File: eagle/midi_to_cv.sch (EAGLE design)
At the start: 45 parts, among them IC2 4504N, IC3 4099N, U1 ATMEGA328P_PDIP

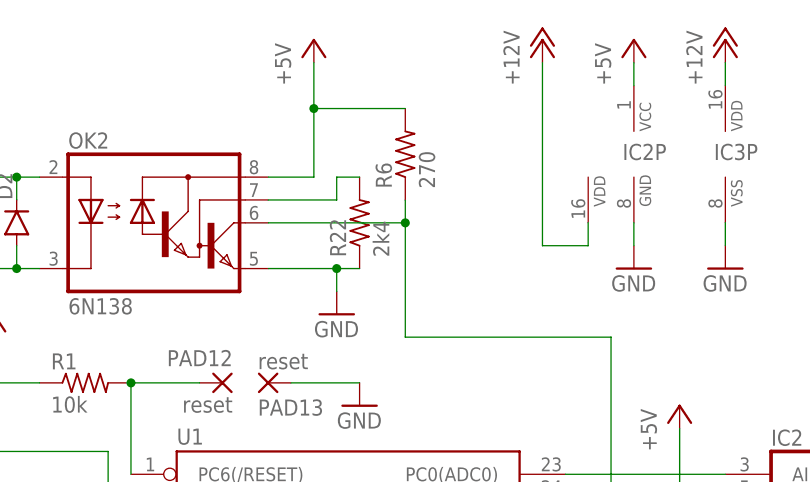
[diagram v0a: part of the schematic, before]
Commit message: wider traces and starting distro board
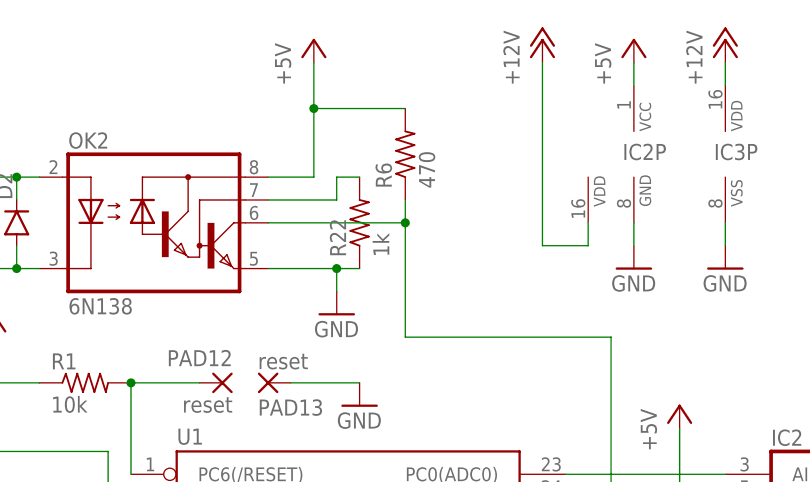
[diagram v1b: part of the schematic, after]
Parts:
- R22: value 2k4 -> 1k
- R6: value 270 -> 470
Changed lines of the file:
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@@
 <?xml version="1.0" encoding="utf-8"?>
 <!DOCTYPE eagle SYSTEM "eagle.dtd">
-<eagle version="7.2.0">
+<eagle version="7.1.0">
 <drawing>
 <settings>
@@
 <part name="D2" library="SparkFun-DiscreteSemi" deviceset="DIODE" device="1N4148"/>
 <part name="R5" library="rcl" deviceset="R-US_" device="0207/10" value="220"/>
-<part name="R6" library="rcl" deviceset="R-US_" device="0207/10" value="270"/>
+<part name="R6" library="rcl" deviceset="R-US_" device="0207/10" value="470"/>
 <part name="P+6" library="supply1" deviceset="+5V" device=""/>
 <part name="MIDI_IN" library="con-molex" deviceset="22-23-2021" device=""/>
@@
 <part name="JP2" library="pinhead" deviceset="PINHD-1X8" device=""/>
 <part name="JP3" library="pinhead" deviceset="PINHD-1X8" device=""/>
-<part name="R22" library="rcl" deviceset="R-US_" device="0207/10" value="2k4"/>
+<part name="R22" library="rcl" deviceset="R-US_" device="0207/10" value="1k"/>
 <part name="LED" library="con-molex" deviceset="22-23-2021" device=""/>
 <part name="GND1" library="supply1" deviceset="GND" device=""/>

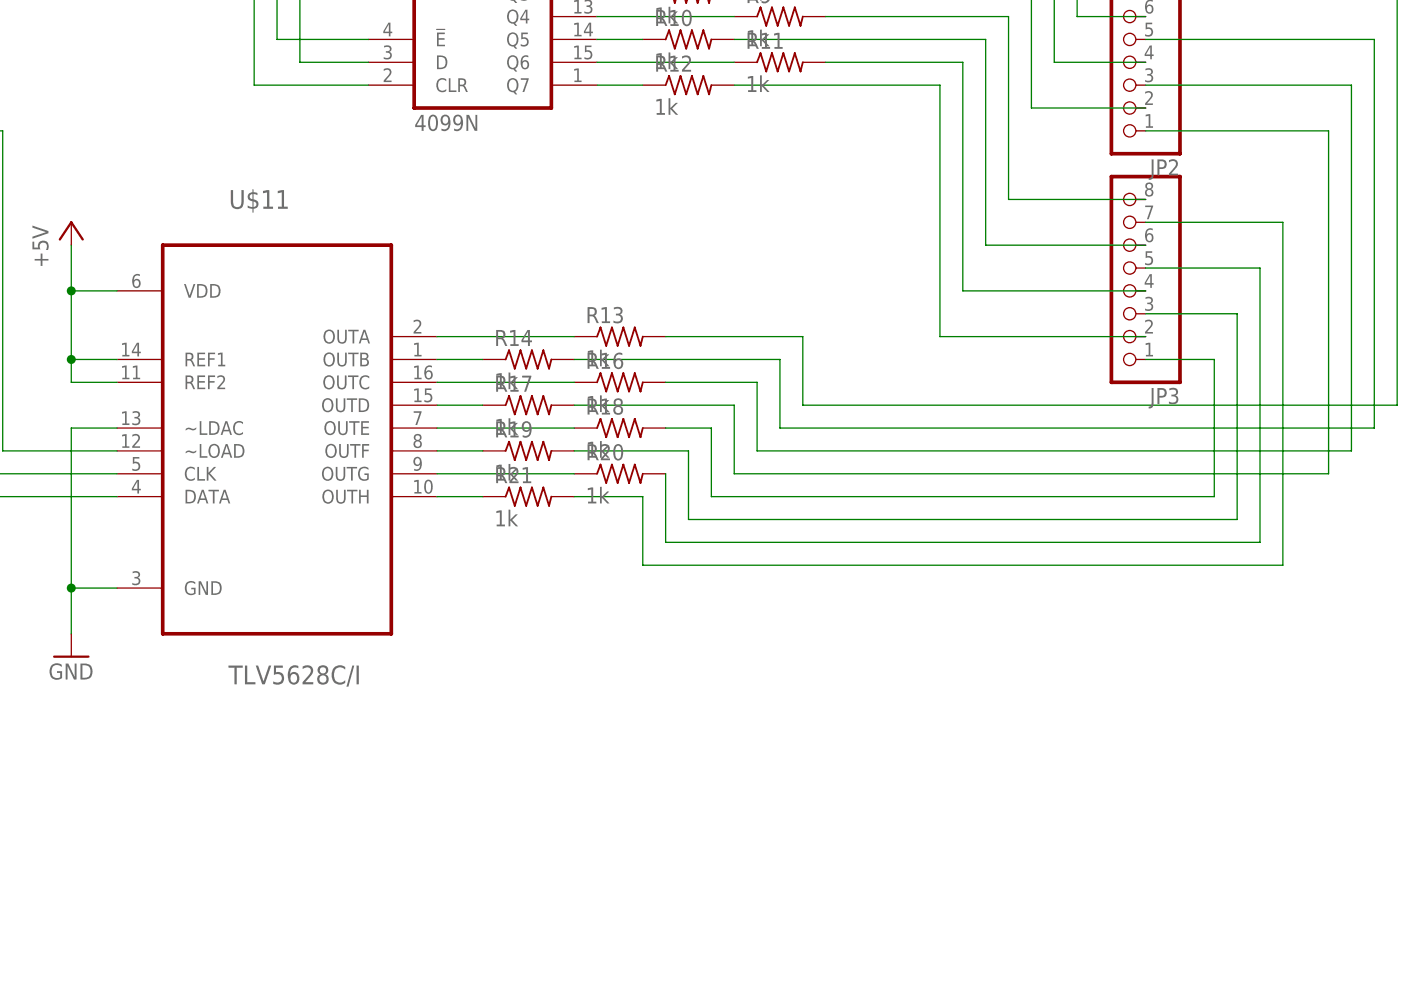
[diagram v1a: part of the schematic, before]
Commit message: adding opamps
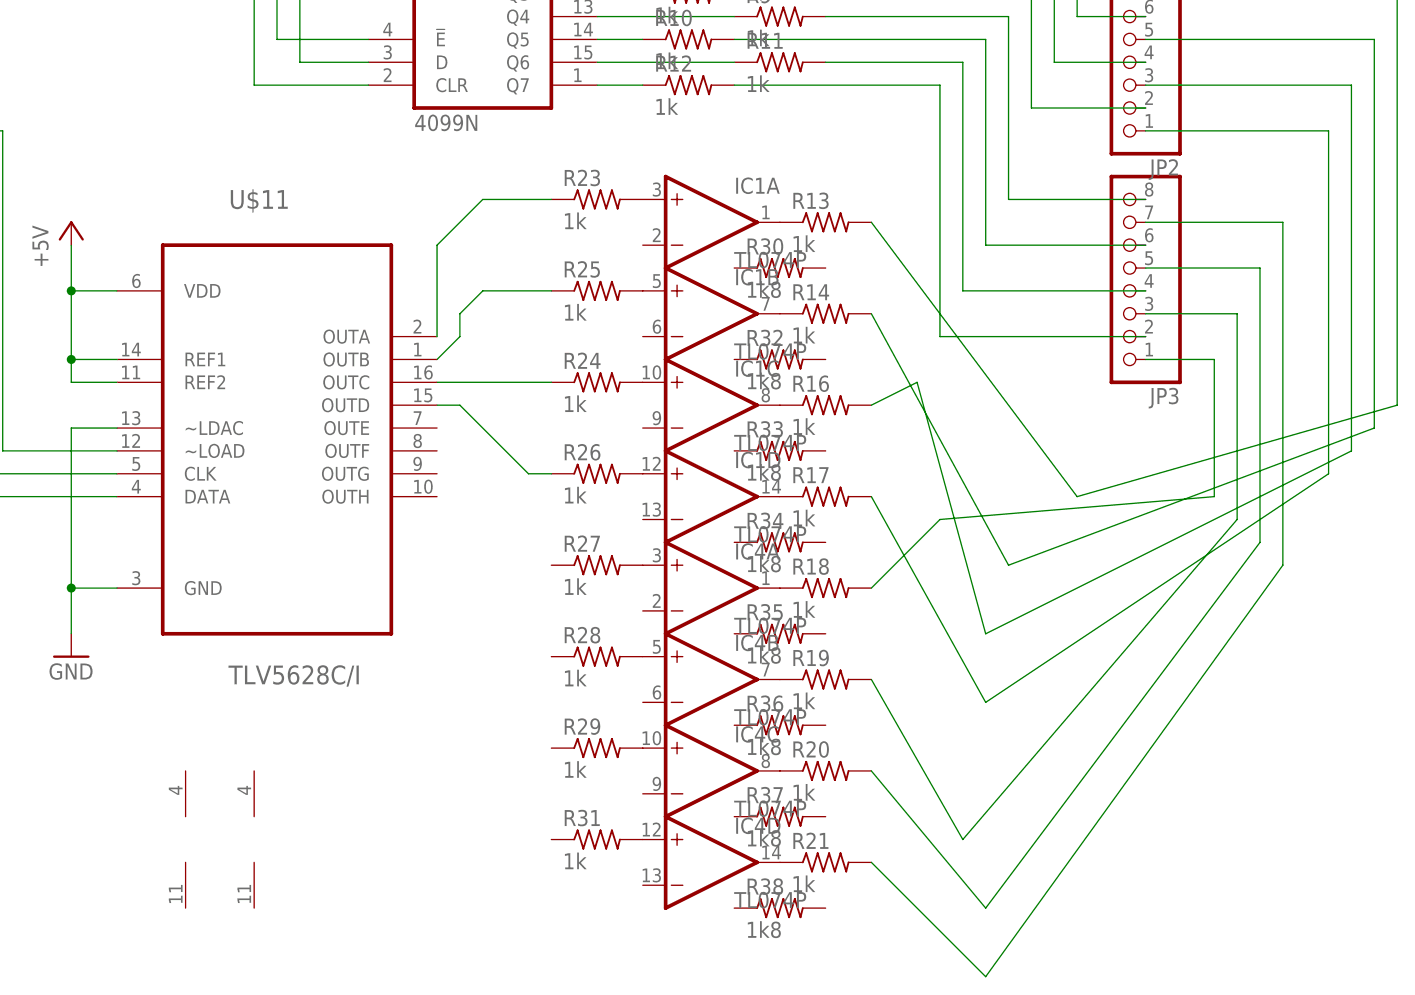
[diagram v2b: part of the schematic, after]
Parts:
- added IC1, IC4: TL074P, linear:TL074P
- added R23, R24, R25, R26, R27, R28, R29, R31: 1k, rcl:R-US_0207/10
- added R30, R32, R33, R34, R35, R36, R37, R38: 1k8, rcl:R-US_0207/10
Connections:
- new net N$26: IC4D.OUT, R21.1
- new net N$42: IC4C.OUT, R20.1
- new net N$43: IC4B.OUT, R19.1
- new net N$63: IC1B.+IN, R25.2
- new net N$64: IC1D.+IN, R26.2
- new net N$65: IC4B.+IN, R28.2
- new net N$66: IC4C.+IN, R29.2
- new net N$67: R23.1, U$11.OUTA
- new net N$68: IC4D.+IN, R31.2
- new net N$69: R25.1, U$11.OUTB
- new net N$70: R24.1, U$11.OUTC
- new net N$71: R26.1, U$11.OUTD
- net N$52: now also IC4A.OUT, R18.1; no longer R13.1, U$11.OUTA
- net N$53: now also IC1D.OUT, R17.1; no longer R14.1, U$11.OUTB
- net N$54: now also IC1C.OUT; no longer U$11.OUTC
- net N$55: now also IC1A.OUT, R13.1; no longer R17.1, U$11.OUTD
- net N$56: now also IC1B.OUT, R14.1; no longer R18.1, U$11.OUTE
- net N$57: now also IC1A.+IN, R23.2; no longer R19.1, U$11.OUTF
- net N$58: now also IC1C.+IN, R24.2; no longer R20.1, U$11.OUTG
- net N$59: now also IC4A.+IN, R27.2; no longer R21.1, U$11.OUTH
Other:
- moved on the sheet: R13, R14, R16, R17, R18, R19, R20, R21

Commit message: feedbacks in place
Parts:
- removed R13, R14, R16, R17, R18, R19, R20, R21: 1k, rcl:R-US_0207/10
- added C10, C11, C8, C9: 100n, rcl:C-US050-024X044
- R30, R32, R33, R34, R35, R36, R37, R38: device rcl:R-US_0207/10 -> rcl:R-US_0204/2V
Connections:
- removed net N$40: JP3.1, R18.2
- removed net N$42: IC4C.OUT, R20.1
- net +12V: now also C10.1, C8.1, IC1P.V+, IC4P.V+
- net GND: now also C11.2, C9.2, IC1P.V-, IC4P.V-, R23.1, R24.1, R25.1, R26.1, R27.1, R28.1, R29.1, R31.1
- net N$22: now also IC1A.OUT, R30.2; no longer R13.2
- net N$24: now also C8.2, C9.1; no longer JP2.5, R14.2
- net N$26: now also C10.2, C11.1; no longer IC4D.OUT, R21.1
- net N$28: now also IC1C.OUT, R33.2; no longer R16.2
- net N$29: now also IC1D.OUT, R34.2; no longer R17.2
- net N$34: now also IC4C.OUT, R37.2; no longer R20.2
- net N$41: now also IC4B.OUT, R36.2; no longer R19.2
- net N$43: now also IC4D.+IN, U$11.OUTH; no longer IC4B.OUT, R19.1
- net N$51: now also IC4D.OUT, R38.2; no longer R21.2
- net N$52: now also JP3.1, R35.2; no longer R18.1
- net N$53: now also IC4C.+IN, U$11.OUTG; no longer IC1D.OUT, R17.1
- net N$54: now also IC4B.+IN, U$11.OUTF; no longer IC1C.OUT, R16.1
- net N$55: now also IC4A.+IN, U$11.OUTE; no longer IC1A.OUT, R13.1
- net N$56: now also JP2.5, R32.2; no longer R14.1
- net N$57: now also IC1A.-IN, R30.1; no longer IC1A.+IN
- net N$58: now also IC1C.-IN, R33.1; no longer IC1C.+IN
- net N$59: now also IC1B.-IN, R25.2, R32.1; no longer IC4A.+IN, R27.2
- net N$63: now also IC1D.-IN, R26.2, R34.1; no longer IC1B.+IN, R25.2
- net N$64: now also IC4A.-IN, R27.2, R35.1; no longer IC1D.+IN, R26.2
- net N$65: now also IC4B.-IN, R36.1; no longer IC4B.+IN
- net N$66: now also IC4C.-IN, R37.1; no longer IC4C.+IN
- net N$67: now also IC4D.-IN, R31.2, R38.1; no longer R23.1, U$11.OUTA
- net N$68: now also IC1D.+IN, U$11.OUTD; no longer IC4D.+IN, R31.2
- net N$69: now also IC1C.+IN, U$11.OUTC; no longer R25.1, U$11.OUTB
- net N$70: now also IC1B.+IN, U$11.OUTB; no longer R24.1, U$11.OUTC
- net N$71: now also IC1A.+IN, U$11.OUTA; no longer R26.1, U$11.OUTD
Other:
- moved on the sheet: IC1A, IC1B, IC1C, IC1D, IC4A, IC4B, IC4C, IC4D, JP2, JP3, R10, R11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

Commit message: started routing
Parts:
- removed C10, C8: 100n, rcl:C-US050-024X044
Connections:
- removed net N$24: C8.2, C9.1
- removed net N$26: C10.2, C11.1
- net +12V: now also C11.1, C9.1; no longer C10.1, C8.1
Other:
- moved on the sheet: C11, C9
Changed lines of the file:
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@@
 <part name="R37" library="rcl" deviceset="R-US_" device="0204/2V" value="1k8"/>
 <part name="R38" library="rcl" deviceset="R-US_" device="0204/2V" value="1k8"/>
-<part name="C8" library="rcl" deviceset="C-US" device="050-024X044" value="100n"/>
 <part name="C9" library="rcl" deviceset="C-US" device="050-024X044" value="100n"/>
-<part name="C10" library="rcl" deviceset="C-US" device="050-024X044" value="100n"/>
 <part name="C11" library="rcl" deviceset="C-US" device="050-024X044" value="100n"/>
 <part name="P+2" library="supply1" deviceset="+12V" device=""/>
@@
 <instance part="R37" gate="G$1" x="149.86" y="-53.34"/>
 <instance part="R38" gate="G$1" x="149.86" y="-63.5"/>
-<instance part="C8" gate="G$1" x="68.58" y="-48.26"/>
-<instance part="C9" gate="G$1" x="68.58" y="-60.96"/>
-<instance part="C10" gate="G$1" x="93.98" y="-48.26"/>
-<instance part="C11" gate="G$1" x="93.98" y="-60.96"/>
+<instance part="C9" gate="G$1" x="68.58" y="-55.88"/>
+<instance part="C11" gate="G$1" x="93.98" y="-55.88"/>
 <instance part="P+2" gate="1" x="78.74" y="-40.64"/>
 <instance part="GND9" gate="1" x="78.74" y="-71.12"/>
@@
 </segment>
 <segment>
-<pinref part="C8" gate="G$1" pin="1"/>
 <pinref part="P+2" gate="1" pin="+12V"/>
 <wire x1="68.58" y1="-45.72" x2="78.74" y2="-45.72" width="0.1524" layer="91"/>
@@
 <wire x1="86.36" y1="-48.26" x2="86.36" y2="-45.72" width="0.1524" layer="91"/>
 <wire x1="86.36" y1="-45.72" x2="78.74" y2="-45.72" width="0.1524" layer="91"/>
-<pinref part="C10" gate="G$1" pin="1"/>
 <wire x1="93.98" y1="-45.72" x2="86.36" y2="-45.72" width="0.1524" layer="91"/>
 <junction x="86.36" y="-45.72"/>
+<pinref part="C9" gate="G$1" pin="1"/>
+<wire x1="68.58" y1="-45.72" x2="68.58" y2="-53.34" width="0.1524" layer="91"/>
+<pinref part="C11" gate="G$1" pin="1"/>
+<wire x1="93.98" y1="-53.34" x2="93.98" y2="-45.72" width="0.1524" layer="91"/>
 </segment>
 </net>
@@
 <pinref part="C9" gate="G$1" pin="2"/>
 <pinref part="IC1" gate="P" pin="V-"/>
+<wire x1="68.58" y1="-60.96" x2="68.58" y2="-66.04" width="0.1524" layer="91"/>
 <wire x1="68.58" y1="-66.04" x2="78.74" y2="-66.04" width="0.1524" layer="91"/>
 <wire x1="78.74" y1="-66.04" x2="78.74" y2="-63.5" width="0.1524" layer="91"/>
@@
 <junction x="78.74" y="-66.04"/>
 <pinref part="C11" gate="G$1" pin="2"/>
+<wire x1="93.98" y1="-60.96" x2="93.98" y2="-66.04" width="0.1524" layer="91"/>
 <wire x1="93.98" y1="-66.04" x2="86.36" y2="-66.04" width="0.1524" layer="91"/>
 <junction x="86.36" y="-66.04"/>
@@
 </segment>
 </net>
-<net name="N$24" class="0">
-<segment>
-<pinref part="C8" gate="G$1" pin="2"/>
-<pinref part="C9" gate="G$1" pin="1"/>
-<wire x1="68.58" y1="-53.34" x2="68.58" y2="-58.42" width="0.1524" layer="91"/>
-</segment>
-</net>
-<net name="N$26" class="0">
-<segment>
-<pinref part="C10" gate="G$1" pin="2"/>
-<pinref part="C11" gate="G$1" pin="1"/>
-<wire x1="93.98" y1="-58.42" x2="93.98" y2="-53.34" width="0.1524" layer="91"/>
-</segment>
-</net>

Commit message: reverted to working midi board
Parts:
- removed C11, C9: 100n, rcl:C-US050-024X044
- removed IC1, IC4: TL074P, linear:TL074P
- removed R23, R24, R25, R26, R27, R28, R29, R31: 1k, rcl:R-US_0207/10
- removed R30, R32, R33, R34, R35, R36, R37, R38: 1k8, rcl:R-US_0204/2V
- added R13, R14, R16, R17, R18, R19, R20, R21: 1k, rcl:R-US_0207/10
- R22: value 1k -> 2k4
- R6: value 470 -> 270
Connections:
- removed net N$43: IC4D.+IN, U$11.OUTH
- removed net N$63: IC1D.-IN, R26.2, R34.1
- removed net N$64: IC4A.-IN, R27.2, R35.1
- removed net N$65: IC4B.-IN, R28.2, R36.1
- removed net N$66: IC4C.-IN, R29.2, R37.1
- removed net N$67: IC4D.-IN, R31.2, R38.1
- removed net N$68: IC1D.+IN, U$11.OUTD
- removed net N$69: IC1C.+IN, U$11.OUTC
- removed net N$70: IC1B.+IN, U$11.OUTB
- removed net N$71: IC1A.+IN, U$11.OUTA
- new net N$24: JP2.5, R14.2
- new net N$40: JP3.1, R18.2
- net +12V: no longer C11.1, C9.1, IC1P.V+, IC4P.V+
- net GND: no longer C11.2, C9.2, IC1P.V-, IC4P.V-, R23.1, R24.1, R25.1, R26.1, R27.1, R28.1, R29.1, R31.1
- net N$22: now also R13.2; no longer IC1A.OUT, R30.2
- net N$28: now also R16.2; no longer IC1C.OUT, R33.2
- net N$29: now also R17.2; no longer IC1D.OUT, R34.2
- net N$34: now also R20.2; no longer IC4C.OUT, R37.2
- net N$41: now also R19.2; no longer IC4B.OUT, R36.2
- net N$51: now also R21.2; no longer IC4D.OUT, R38.2
- net N$52: now also R13.1, U$11.OUTA; no longer IC4A.OUT, JP3.1, R35.2
- net N$53: now also R14.1, U$11.OUTB; no longer IC4C.+IN, U$11.OUTG
- net N$54: now also R16.1, U$11.OUTC; no longer IC4B.+IN, U$11.OUTF
- net N$55: now also R17.1, U$11.OUTD; no longer IC4A.+IN, U$11.OUTE
- net N$56: now also R18.1, U$11.OUTE; no longer IC1B.OUT, JP2.5, R32.2
- net N$57: now also R19.1, U$11.OUTF; no longer IC1A.-IN, R23.2, R30.1
- net N$58: now also R20.1, U$11.OUTG; no longer IC1C.-IN, R24.2, R33.1
- net N$59: now also R21.1, U$11.OUTH; no longer IC1B.-IN, R25.2, R32.1
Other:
- moved on the sheet: JP2, JP3, R10, R11, R12, R2, R3, R7, R8, R9
